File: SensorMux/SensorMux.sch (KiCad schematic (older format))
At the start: 0 parts

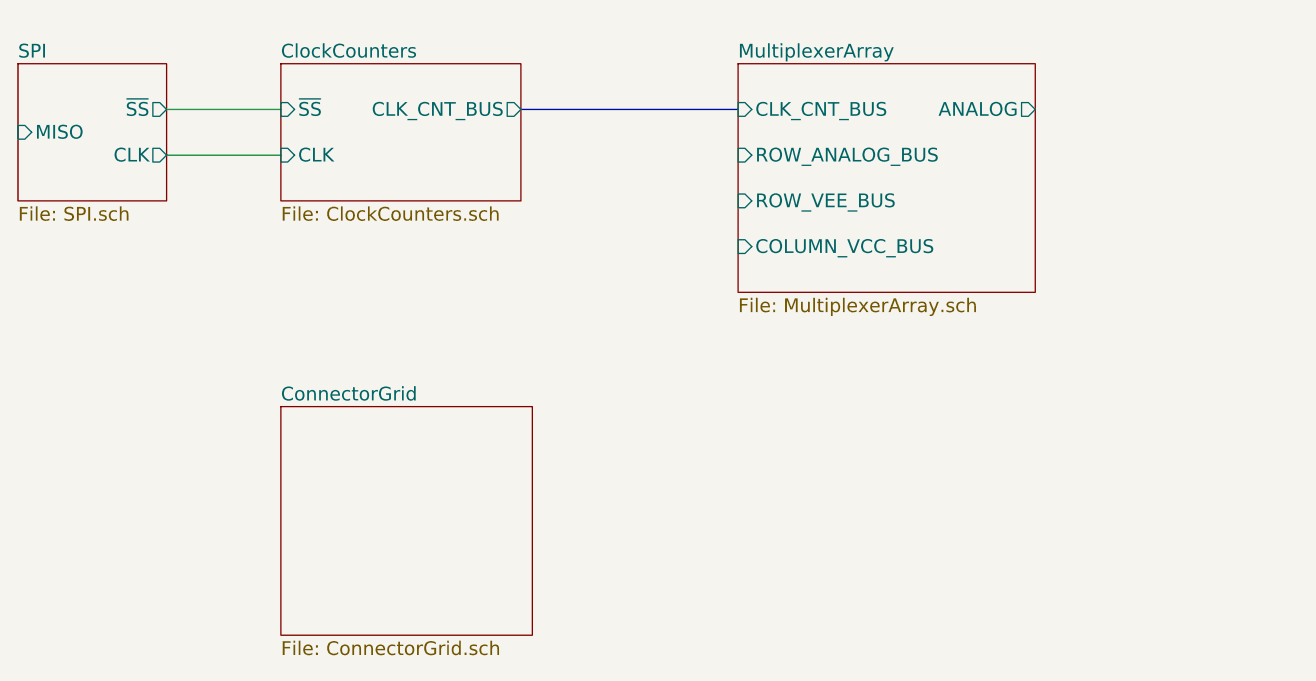
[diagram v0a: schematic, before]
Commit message: Added sensor grid schematics.
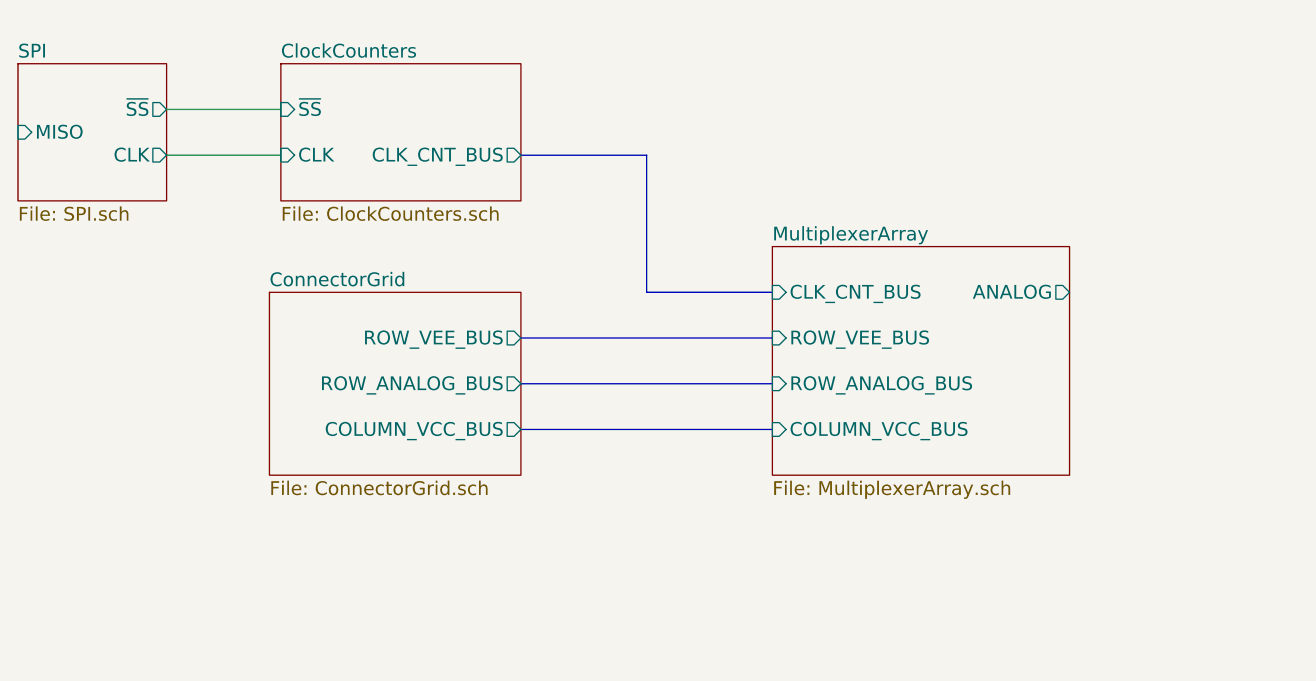
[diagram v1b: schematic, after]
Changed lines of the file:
@@
 LIBS:contrib
 LIBS:valves
-LIBS:Trainiot
 LIBS:SensorMux-cache
 EELAYER 25 0
@@
 F2 "~SS" I L 2300 3700 60
 F3 "CLK" I L 2300 3900 60
-F4 "CLK_CNT_BUS" O R 3350 3700 60
+F4 "CLK_CNT_BUS" O R 3350 3900 60
 $EndSheet
 $Sheet
@@
 $EndSheet
 $Sheet
-S 4300 3500 1300 1000
+S 4450 4300 1300 1000
 U 5A4ABEE0
 F0 "MultiplexerArray" 60
 F1 "MultiplexerArray.sch" 60
-F2 "CLK_CNT_BUS" I L 4300 3700 60
-F3 "ANALOG" O R 5600 3700 60
-F4 "COLUMN_VCC_BUS" I L 4300 4300 60
-F5 "ROW_ANALOG_BUS" I L 4300 3900 60
-F6 "ROW_VEE_BUS" I L 4300 4100 60
+F2 "CLK_CNT_BUS" I L 4450 4500 60
+F3 "ANALOG" O R 5750 4500 60
+F4 "COLUMN_VCC_BUS" I L 4450 5100 60
+F5 "ROW_ANALOG_BUS" I L 4450 4900 60
+F6 "ROW_VEE_BUS" I L 4450 4700 60
 $EndSheet
 $Sheet
-S 2300 5000 1100 1000
+S 2250 4500 1100 800
 U 5A4B6DDC
 F0 "ConnectorGrid" 60
 F1 "ConnectorGrid.sch" 60
+F2 "ROW_VEE_BUS" O R 3350 4700 60
+F3 "ROW_ANALOG_BUS" O R 3350 4900 60
+F4 "COLUMN_VCC_BUS" O R 3350 5100 60
 $EndSheet
 Wire Wire Line
@@
 	1800 3900 2300 3900
 Wire Bus Line
-	3350 3700 4300 3700
+	3350 3900 3900 3900
+Wire Bus Line
+	3900 3900 3900 4500
+Wire Bus Line
+	3900 4500 4450 4500
+Wire Bus Line
+	4450 4700 3350 4700
+Wire Bus Line
+	3350 4900 4450 4900
+Wire Bus Line
+	3350 5100 4450 5100
 $EndSCHEMATC

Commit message: Addel labels to the wires in the sensor grid.
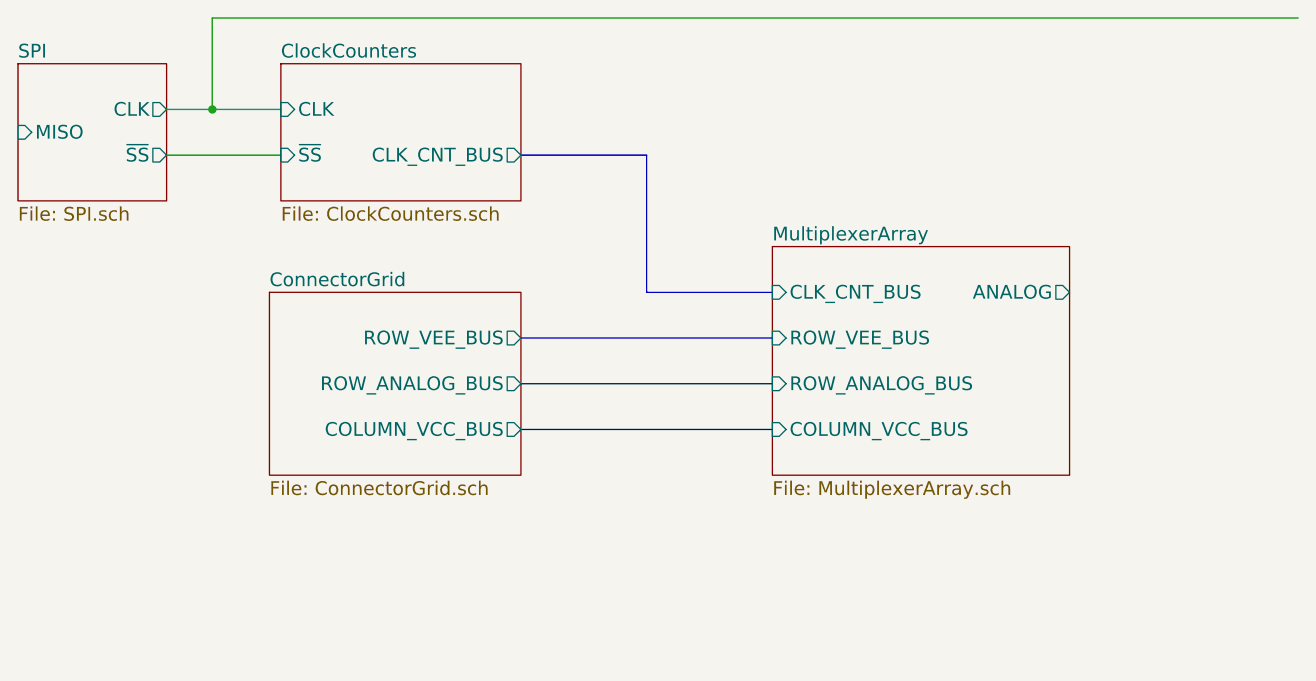
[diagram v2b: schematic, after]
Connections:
- wire segments 2 -> 4
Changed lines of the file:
@@
 F0 "ClockCounters" 60
 F1 "ClockCounters.sch" 60
-F2 "~SS" I L 2300 3700 60
-F3 "CLK" I L 2300 3900 60
+F2 "~SS" I L 2300 3900 60
+F3 "CLK" I L 2300 3700 60
 F4 "CLK_CNT_BUS" O R 3350 3900 60
 $EndSheet
@@
 F1 "SPI.sch" 60
 F2 "MISO" I L 1150 3800 60
-F3 "~SS" O R 1800 3700 60
-F4 "CLK" O R 1800 3900 60
+F3 "~SS" O R 1800 3900 60
+F4 "CLK" O R 1800 3700 60
 $EndSheet
 $Sheet
@@
 Wire Bus Line
 	3350 5100 4450 5100
+Wire Wire Line
+	2000 3700 2000 3300
+Wire Wire Line
+	2000 3300 6750 3300
+Connection ~ 2000 3700
 $EndSCHEMATC
